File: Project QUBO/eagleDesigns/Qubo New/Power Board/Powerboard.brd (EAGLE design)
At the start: 160 x 100 mm, 45 parts, among them IC1 PCF8574T, U1 UEI15

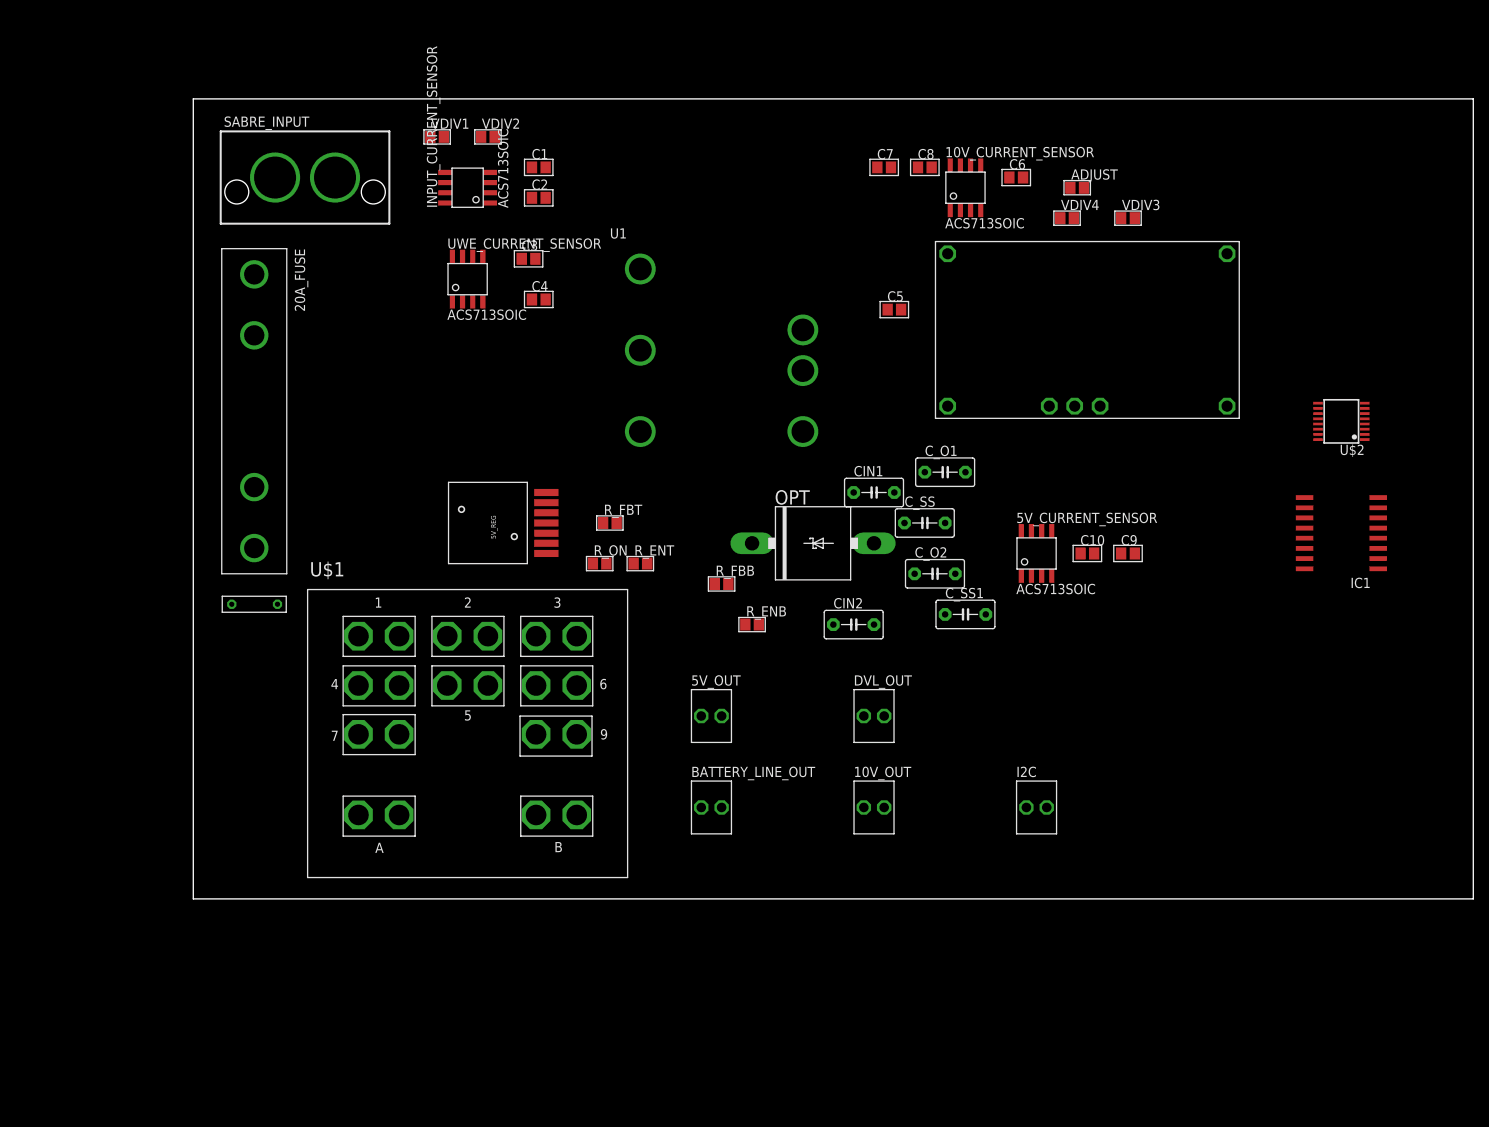
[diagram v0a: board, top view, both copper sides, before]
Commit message: 
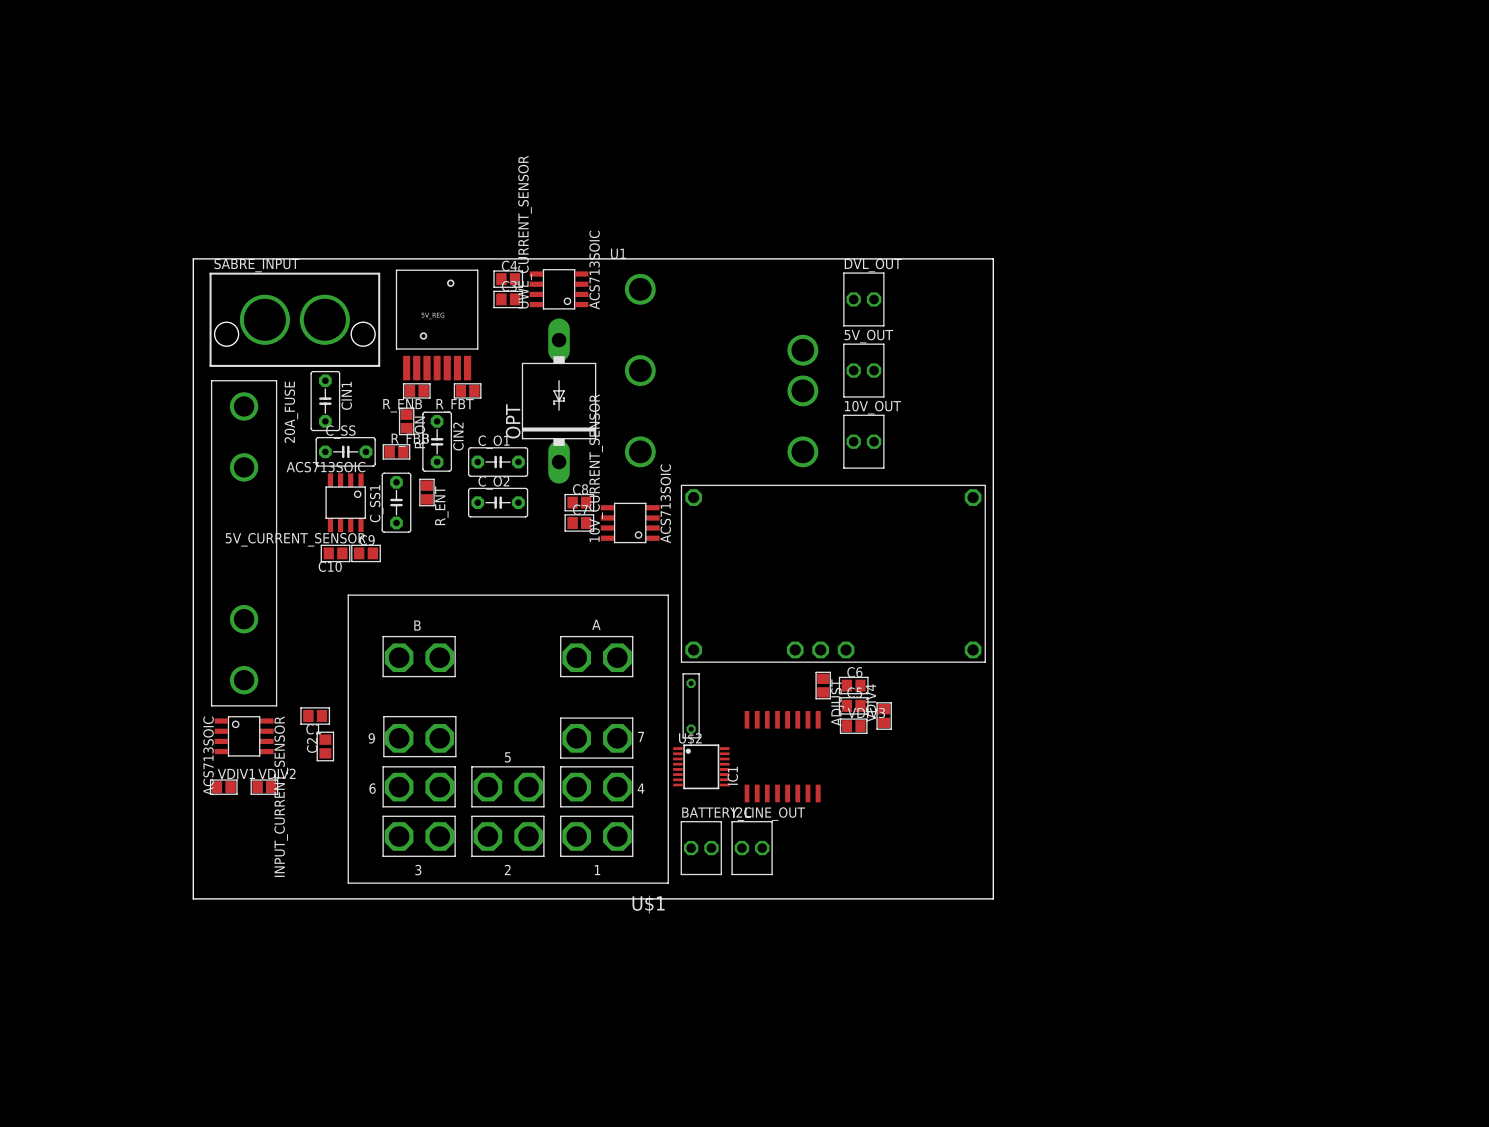
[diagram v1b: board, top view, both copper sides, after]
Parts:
- moved C9 95.2 mm to (21.6, 43.2)
- moved C10 94.0 mm to (17.8, 43.2), turned to 180 degrees
- moved U$2 90.9 mm to (63.5, 16.5), turned to 270 degrees
- moved 5V_CURRENT_SENSOR 86.6 mm to (19.1, 49.5), turned to 180 degrees
- moved VDIV2 85.9 mm to (8.89, 14.0)
- moved VDIV1 85.5 mm to (3.81, 14.0)
- moved IC1 75.2 mm to (73.7, 17.8), turned to 0 degrees
- moved INPUT_CURRENT_SENSOR 74.1 mm to (6.35, 20.3), turned to 270 degrees
- moved C1 74.1 mm to (15.2, 22.9), turned to 180 degrees
- moved C2 73.6 mm to (16.5, 19.1), turned to 90 degrees
- moved C_SS 72.9 mm to (19.1, 55.9)
- moved C_SS1 72.5 mm to (25.4, 49.5), turned to 90 degrees
- moved VDIV3 72.2 mm to (82.5, 21.6)
- moved ADJUST 69.9 mm to (78.7, 26.7), turned to 270 degrees
- moved CIN1 69.5 mm to (16.5, 62.2), turned to 270 degrees
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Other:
- board size 160 x 100 mm -> 100 x 80 mm

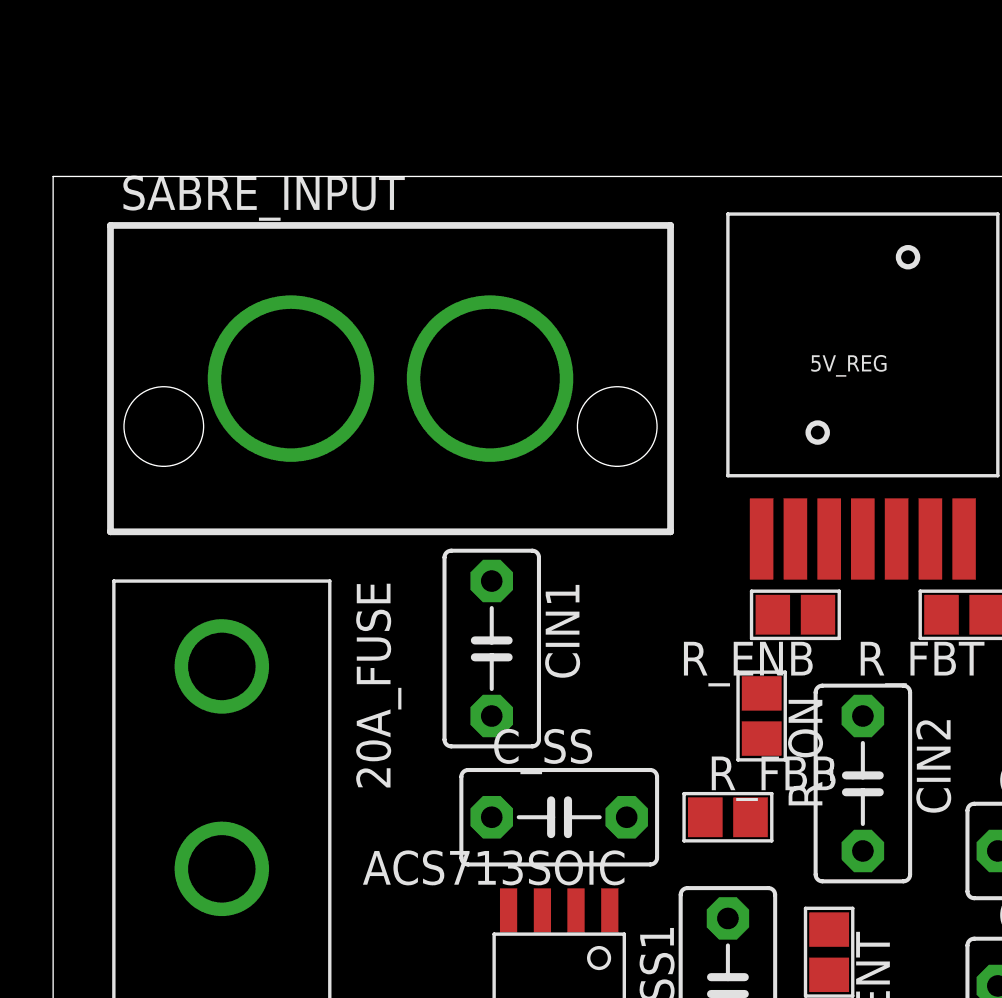
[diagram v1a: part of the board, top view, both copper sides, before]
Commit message: 
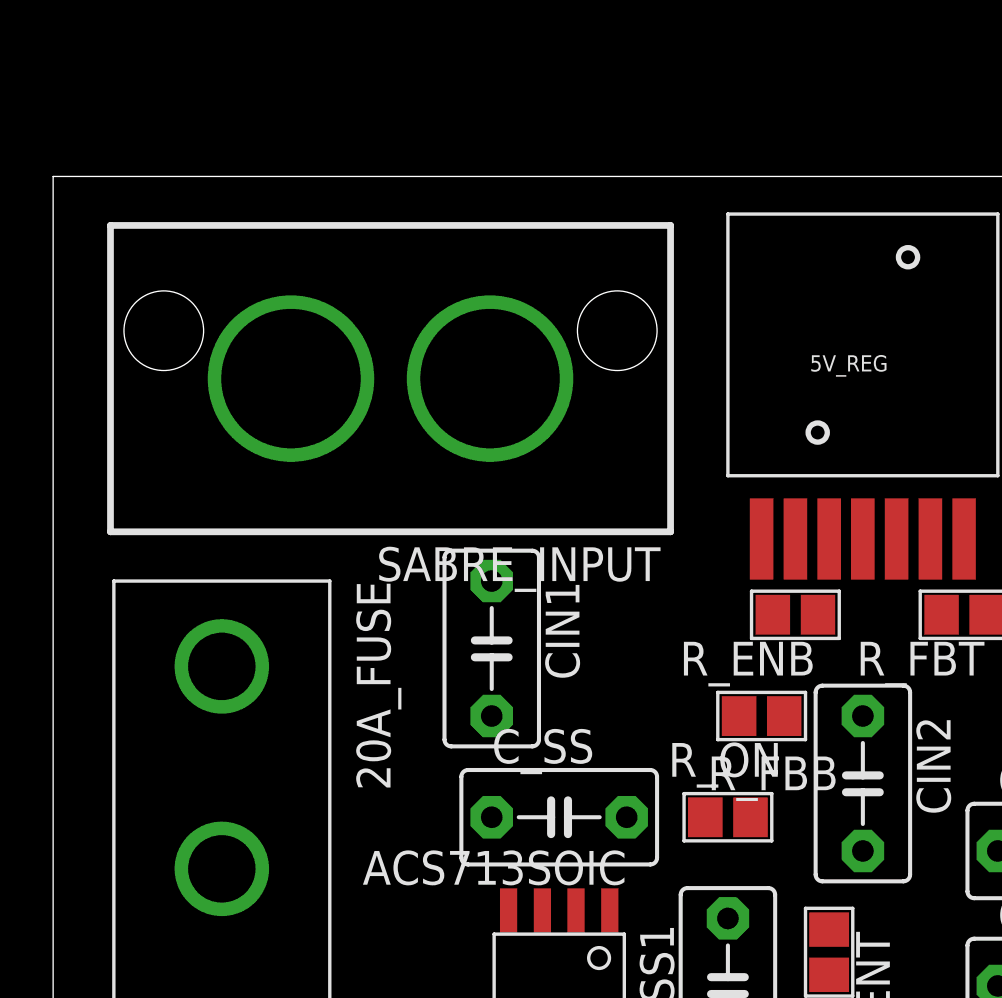
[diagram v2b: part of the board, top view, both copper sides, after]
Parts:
- turned R_ON to 180 degrees
- turned SABRE_INPUT to 180 degrees
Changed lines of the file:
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@@
 <element name="R_FBB" library="resistor" package="R0805" value="" x="25.4" y="55.88"/>
 <element name="R_FBT" library="resistor" package="R0805" value="" x="34.29" y="63.5" rot="R180"/>
-<element name="R_ON" library="resistor" package="R0805" value="" x="26.67" y="59.69" rot="R270"/>
-<element name="SABRE_INPUT" library="molex" package="SUPERSABRE_2CIRCUIT" value="2_SUPERSABRE" x="12.7" y="72.39"/>
+<element name="R_ON" library="resistor" package="R0805" value="" x="26.67" y="59.69" rot="R180"/>
+<element name="SABRE_INPUT" library="molex" package="SUPERSABRE_2CIRCUIT" value="2_SUPERSABRE" x="12.7" y="72.39" rot="R180"/>
 <element name="U$1" library="TE" package="KUHP_6.35MM-QUICK-CONNECT" value="KUHP-5XX1-XX" x="39.37" y="13.97" rot="R180"/>
 <element name="U$2" library="texas" package="TSSOP16" value="ADS7828" x="63.5" y="16.51" rot="R270"/>
@@
 <contactref element="20A_FUSE" pad="P$1"/>
 <contactref element="20A_FUSE" pad="P$2"/>
-<wire x1="6.35" y1="61.5569" x2="16.4465" y2="72.39" width="0" layer="19" extent="1-1"/>
+<wire x1="6.35" y1="61.5569" x2="8.9535" y2="72.39" width="0" layer="19" extent="1-1"/>
 <wire x1="6.35" y1="53.9369" x2="6.35" y2="61.5569" width="0" layer="19" extent="1-1"/>
 </signal>
@@
 <wire x1="20.74" y1="43.18" x2="18.63" y2="43.18" width="0" layer="19" extent="1-1"/>
 <wire x1="17.145" y1="46.73" x2="18.63" y2="43.18" width="0" layer="19" extent="1-1"/>
-<wire x1="38.52" y1="74.93" x2="47.41" y2="49.53" width="0" layer="19" extent="1-1"/>
+<wire x1="16.4465" y1="72.39" x2="17.145" y2="46.73" width="0" layer="19" extent="1-1"/>
+<wire x1="38.52" y1="74.93" x2="16.4465" y2="72.39" width="0" layer="19" extent="1-1"/>
 <wire x1="38.52" y1="77.47" x2="38.52" y2="74.93" width="0" layer="19" extent="1-1"/>
 <wire x1="42.92" y1="78.105" x2="38.52" y2="77.47" width="0" layer="19" extent="1-1"/>
-<wire x1="8.9535" y1="72.39" x2="17.145" y2="46.73" width="0" layer="19" extent="1-1"/>
 </signal>
 <signal name="N$1">
@@
 <wire x1="26.67" y1="66.355" x2="30.48" y2="66.355" width="0" layer="19" extent="1-1"/>
 <wire x1="27.09" y1="63.5" x2="26.67" y2="66.355" width="0" layer="19" extent="1-1"/>
-<wire x1="26.67" y1="58.84" x2="27.09" y2="63.5" width="0" layer="19" extent="1-1"/>
-<wire x1="24.55" y1="55.88" x2="26.67" y2="58.84" width="0" layer="19" extent="1-1"/>
-<wire x1="30.48" y1="59.69" x2="26.67" y2="58.84" width="0" layer="19" extent="1-1"/>
+<wire x1="25.82" y1="59.69" x2="27.09" y2="63.5" width="0" layer="19" extent="1-1"/>
+<wire x1="24.55" y1="55.88" x2="25.82" y2="59.69" width="0" layer="19" extent="1-1"/>
+<wire x1="30.48" y1="59.69" x2="25.82" y2="59.69" width="0" layer="19" extent="1-1"/>
 <wire x1="20.955" y1="52.33" x2="24.55" y2="55.88" width="0" layer="19" extent="1-1"/>
 <wire x1="19.685" y1="52.33" x2="20.955" y2="52.33" width="0" layer="19" extent="1-1"/>
@@
 <contactref element="R_ON" pad="1"/>
 <contactref element="5V_REG" pad="2"/>
-<wire x1="26.67" y1="60.54" x2="27.94" y2="66.355" width="0" layer="19" extent="1-1"/>
+<wire x1="27.52" y1="59.69" x2="27.94" y2="66.355" width="0" layer="19" extent="1-1"/>
 </signal>
 <signal name="N$3">
